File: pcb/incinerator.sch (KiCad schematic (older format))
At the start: 51 parts, among them J1 IGNITION_MAIN, J2 IGNITION_AFT, J3 VALVE_MAIN, J4 VALVE_AFT_HI, J5 Waveshare 4.2\" e-paper, J6 VALVE_AFT_LO, J7 AIRPMP, J8 Power Source 12V, Q1 IRLU120N, Q2 IRLU120N, Q3 IRLU120N, Q4 IRLU120N, Q5 IRLU120N, Q6 IRLU120N, SW1 Rotary_Encoder_Switch, U1 NodeMCU_ESP32, U2 Adafruit_MAX31855, U3 Adafruit_MAX31855, U4 R-7890-0.5

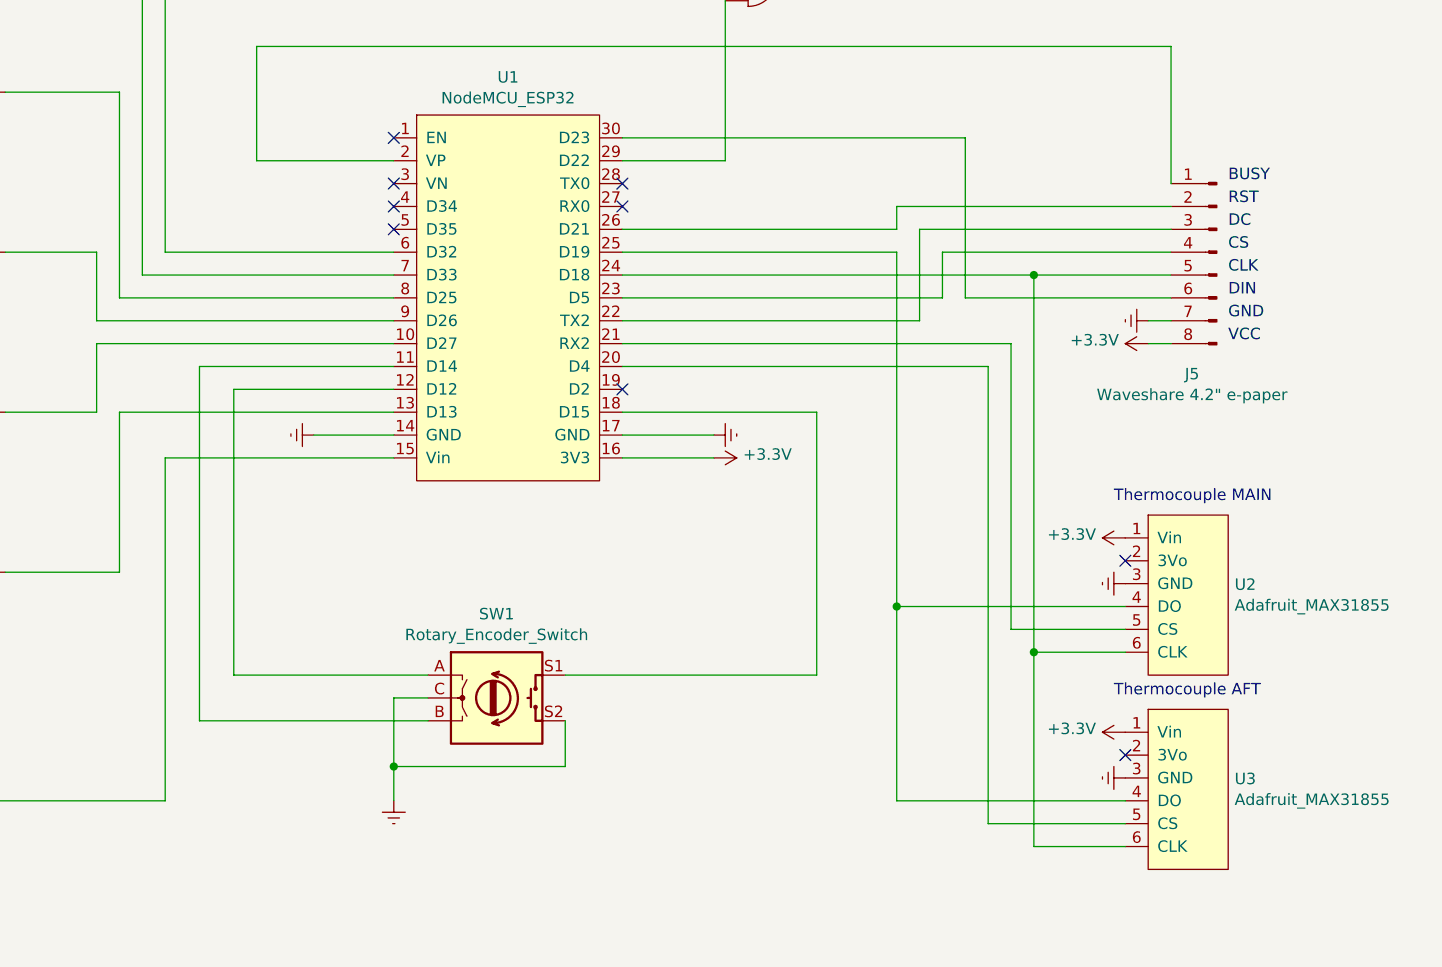
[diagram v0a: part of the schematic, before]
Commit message: Add connector to interface the encoder/switch
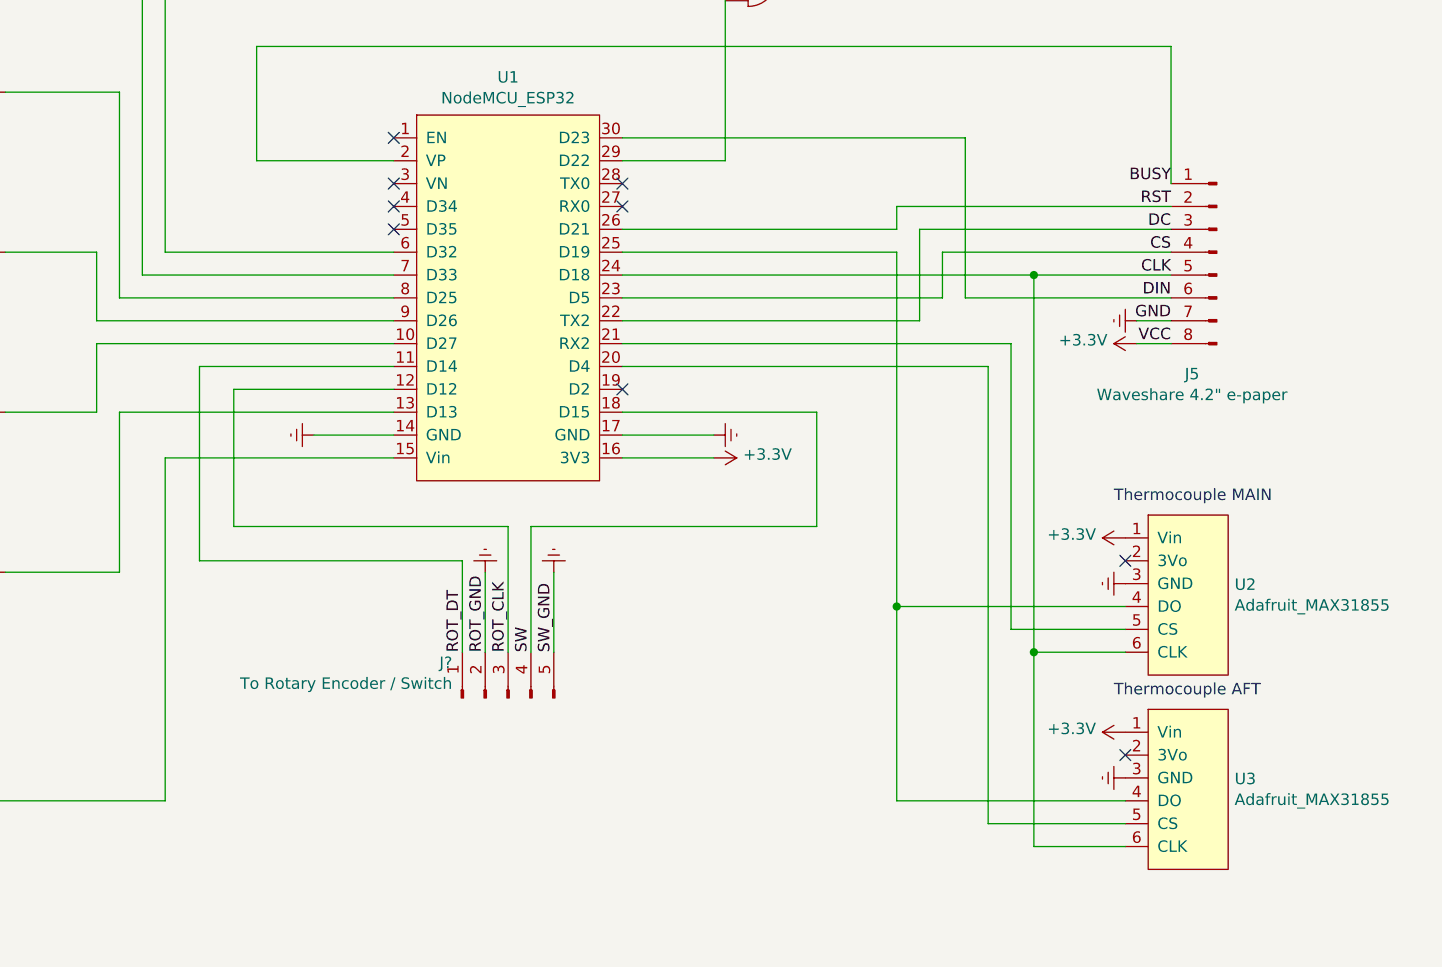
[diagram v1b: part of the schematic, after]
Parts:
- removed SW1: Rotary_Encoder_Switch, symbol Device:Rotary_Encoder_Switch
- added J?: To Rotary Encoder / Switch, symbol Connector:Conn_01x05_Male
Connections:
- net BUSY: now also J5.1 (Pin_1), U1.2 (VP)
- net CLK: now also J5.5 (Pin_5), U1.24 (D18), U2.6 (CLK), U3.6 (CLK)
- net CS: now also J5.4 (Pin_4), U1.23 (D5)
- net DC: now also J5.3 (Pin_3), U1.22 (TX2)
- net DIN: now also J5.6 (Pin_6), U1.30 (D23)
- net Earth: now also J?.2 (Pin_2), J?.5 (Pin_5)
- net RST: now also J5.2 (Pin_2), U1.26 (D21)
- net ROT_CLK: now reaches U1.12 (D12)
- net ROT_CLK: now also J?.3 (Pin_3)
- net ROT_DT: now reaches U1.11 (D14)
- net ROT_DT: now also J?.1 (Pin_1)
- net SW: now reaches U1.18 (D15)
- net SW: now also J?.4 (Pin_4)
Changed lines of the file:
@@
 Comment4 "Author: Patrick Huesmann"
 $EndDescr
-Text Label 10400 3350 0    50   ~ 0
+Text Label 10150 3350 2    50   ~ 0
 BUSY
-Text Label 10400 3450 0    50   ~ 0
+Text Label 10150 3450 2    50   ~ 0
 RST
-Text Label 10400 3550 0    50   ~ 0
+Text Label 10150 3550 2    50   ~ 0
 DC
-Text Label 10400 3650 0    50   ~ 0
+Text Label 10150 3650 2    50   ~ 0
 CS
-Text Label 10400 3750 0    50   ~ 0
+Text Label 10150 3750 2    50   ~ 0
 CLK
-Text Label 10400 3850 0    50   ~ 0
+Text Label 10150 3850 2    50   ~ 0
 DIN
-Text Label 10400 3950 0    50   ~ 0
+Text Label 10150 3950 2    50   ~ 0
 GND
-Text Label 10400 4050 0    50   ~ 0
+Text Label 10150 4050 2    50   ~ 0
 VCC
 Wire Wire Line
@@
 Wire Wire Line
 	9050 3550 9050 3950
-$Comp
-L Device:Rotary_Encoder_Switch SW1
-U 1 1 5DFF2455
-P 7200 5600
-F 0 "SW1" H 7200 5967 50  0000 C CNN
-F 1 "Rotary_Encoder_Switch" H 7200 5876 50  0000 C CNN
-F 2 "" H 7050 5760 50  0001 C CNN
-F 3 "~" H 7200 5860 50  0001 C CNN
-	1    7200 5600
-	1    0    0    -1
-$EndComp
-Wire Wire Line
-	6900 5600 6750 5600
-Wire Wire Line
-	6750 5600 6750 5900
-$Comp
-L power:Earth #PWR024
-U 1 1 5DFFCCE8
-P 6750 6050
-F 0 "#PWR024" H 6750 5800 50  0001 C CNN
-F 1 "Earth" H 6750 5900 50  0001 C CNN
-F 2 "" H 6750 6050 50  0001 C CNN
-F 3 "~" H 6750 6050 50  0001 C CNN
-	1    6750 6050
-	1    0    0    -1
-$EndComp
-Wire Wire Line
-	7500 5700 7500 5900
-Wire Wire Line
-	7500 5900 6750 5900
-Connection ~ 6750 5900
-Wire Wire Line
-	6750 5900 6750 6050
-Wire Wire Line
-	6900 5500 6050 5500
-Wire Wire Line
-	6900 5700 5900 5700
 Connection ~ 9550 3750
 Wire Wire Line
@@
 L power:Earth #PWR010
 U 1 1 5DEEEE26
-P 10050 3950
-F 0 "#PWR010" H 10050 3700 50  0001 C CNN
-F 1 "Earth" H 10050 3800 50  0001 C CNN
-F 2 "" H 10050 3950 50  0001 C CNN
-F 3 "~" H 10050 3950 50  0001 C CNN
-	1    10050 3950
-	0    1    1    0
-$EndComp
-Wire Wire Line
-	10050 3950 10150 3950
+P 10000 3950
+F 0 "#PWR010" H 10000 3700 50  0001 C CNN
+F 1 "Earth" H 10000 3800 50  0001 C CNN
+F 2 "" H 10000 3950 50  0001 C CNN
+F 3 "~" H 10000 3950 50  0001 C CNN
+	1    10000 3950
+	0    1    1    0
+$EndComp
+Wire Wire Line
+	10000 3950 10150 3950
 $Comp
 L Connector:Conn_01x08_Male J5
@@
 L power:+3.3V #PWR011
 U 1 1 5DEFD454
-P 10050 4050
-F 0 "#PWR011" H 10050 3900 50  0001 C CNN
-F 1 "+3.3V" V 10065 4178 50  0000 L CNN
-F 2 "" H 10050 4050 50  0001 C CNN
-F 3 "" H 10050 4050 50  0001 C CNN
-	1    10050 4050
-	0    -1   -1   0
-$EndComp
-Wire Wire Line
-	10050 4050 10150 4050
+P 10000 4050
+F 0 "#PWR011" H 10000 3900 50  0001 C CNN
+F 1 "+3.3V" V 10015 4178 50  0000 L CNN
+F 2 "" H 10000 4050 50  0001 C CNN
+F 3 "" H 10000 4050 50  0001 C CNN
+	1    10000 4050
+	0    -1   -1   0
+$EndComp
+Wire Wire Line
+	10000 4050 10150 4050
 $Comp
 L power:Earth #PWR019
@@
 $EndComp
 Wire Wire Line
-	8600 4350 8600 5500
-Wire Wire Line
-	7500 5500 8600 5500
+	8600 4350 8600 4850
 $Comp
 L power:+3.3V #PWR015
@@
 	6750 4250 6050 4250
 Wire Wire Line
-	6050 4250 6050 5500
+	6050 4250 6050 4850
 Wire Wire Line
 	6750 4150 5900 4150
-Wire Wire Line
-	5900 4150 5900 5700
 $Comp
 L Device:Q_NMOS_GDS Q1
@@
 NoConn ~ 7750 3450
 NoConn ~ 7750 3350
+$Comp
+L power:Earth #PWR?
+U 1 1 5E1FC7FA
+P 7150 5050
+F 0 "#PWR?" H 7150 4800 50  0001 C CNN
+F 1 "Earth" H 7150 4900 50  0001 C CNN
+F 2 "" H 7150 5050 50  0001 C CNN
+F 3 "~" H 7150 5050 50  0001 C CNN
+	1    7150 5050
+	-1   0    0    1
+$EndComp
+$Comp
+L power:Earth #PWR?
+U 1 1 5E1FD446
+P 7450 5050
+F 0 "#PWR?" H 7450 4800 50  0001 C CNN
+F 1 "Earth" H 7450 4900 50  0001 C CNN
+F 2 "" H 7450 5050 50  0001 C CNN
+F 3 "~" H 7450 5050 50  0001 C CNN
+	1    7450 5050
+	-1   0    0    1
+$EndComp
+Wire Wire Line
+	7450 5400 7450 5050
+Wire Wire Line
+	7150 5400 7150 5050
+Text Label 7050 5400 1    50   ~ 0
+ROT_DT
+Text Label 7250 5400 1    50   ~ 0
+ROT_CLK
+Text Label 7350 5400 1    50   ~ 0
+SW
+$Comp
+L Connector:Conn_01x05_Male J?
+U 1 1 5E1A7E2D
+P 7250 5600
+F 0 "J?" V 7404 5844 50  0000 L CNN
+F 1 "To Rotary Encoder / Switch" V 7313 5844 50  0000 L CNN
+F 2 "" H 7250 5600 50  0001 C CNN
+F 3 "~" H 7250 5600 50  0001 C CNN
+	1    7250 5600
+	0    -1   -1   0
+$EndComp
+Wire Wire Line
+	6050 4850 7250 4850
+Wire Wire Line
+	7250 4850 7250 5400
+Wire Wire Line
+	5900 5000 7050 5000
+Wire Wire Line
+	7050 5000 7050 5400
+Wire Wire Line
+	5900 4150 5900 5000
+Wire Wire Line
+	8600 4850 7350 4850
+Wire Wire Line
+	7350 4850 7350 5400
+Text Label 7150 5400 1    50   ~ 0
+ROT_GND
+Text Label 7450 5400 1    50   ~ 0
+SW_GND
 $EndSCHEMATC

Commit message: Re-annotated symbols
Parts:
- gave numbers to parts that had none: 1
- renumbered J8 to J9
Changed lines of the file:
@@
 	10000 4050 10150 4050
 $Comp
-L power:Earth #PWR019
+L power:Earth #PWR021
 U 1 1 5DF0E96B
 P 9950 5100
-F 0 "#PWR019" H 9950 4850 50  0001 C CNN
+F 0 "#PWR021" H 9950 4850 50  0001 C CNN
 F 1 "Earth" H 9950 4950 50  0001 C CNN
 F 2 "" H 9950 5100 50  0001 C CNN
@@
 $EndComp
 $Comp
-L power:Earth #PWR023
+L power:Earth #PWR025
 U 1 1 5DF11219
 P 9950 5950
-F 0 "#PWR023" H 9950 5700 50  0001 C CNN
+F 0 "#PWR025" H 9950 5700 50  0001 C CNN
 F 1 "Earth" H 9950 5800 50  0001 C CNN
 F 2 "" H 9950 5950 50  0001 C CNN
@@
 $EndComp
 $Comp
-L power:+3.3V #PWR021
+L power:+3.3V #PWR024
 U 1 1 5DF11220
 P 9950 5750
-F 0 "#PWR021" H 9950 5600 50  0001 C CNN
+F 0 "#PWR024" H 9950 5600 50  0001 C CNN
 F 1 "+3.3V" V 9965 5878 50  0000 L CNN
 F 2 "" H 9950 5750 50  0001 C CNN
@@
 Connection ~ 4100 1750
 $Comp
-L Connector:Screw_Terminal_01x02 J8
+L Connector:Screw_Terminal_01x02 J9
 U 1 1 5E156F2E
 P 1150 6050
-F 0 "J8" H 1068 6267 50  0000 C CNN
+F 0 "J9" H 1068 6267 50  0000 C CNN
 F 1 "Power Source 12V" H 1068 6176 50  0000 C CNN
 F 2 "" H 1150 6050 50  0001 C CNN
@@
 $EndComp
 $Comp
-L power:Earth #PWR025
+L power:Earth #PWR026
 U 1 1 5E159756
 P 1700 6600
-F 0 "#PWR025" H 1700 6350 50  0001 C CNN
+F 0 "#PWR026" H 1700 6350 50  0001 C CNN
 F 1 "Earth" H 1700 6450 50  0001 C CNN
 F 2 "" H 1700 6600 50  0001 C CNN
@@
 $EndComp
 $Comp
-L power:Earth #PWR020
+L power:Earth #PWR022
 U 1 1 5E319DD4
 P 4100 5350
-F 0 "#PWR020" H 4100 5100 50  0001 C CNN
+F 0 "#PWR022" H 4100 5100 50  0001 C CNN
 F 1 "Earth" H 4100 5200 50  0001 C CNN
 F 2 "" H 4100 5350 50  0001 C CNN
@@
 Connection ~ 1700 6350
 $Comp
-L power:PWR_FLAG #FLG0101
+L power:PWR_FLAG #FLG02
 U 1 1 5E1C89C2
 P 1700 6550
-F 0 "#FLG0101" H 1700 6625 50  0001 C CNN
+F 0 "#FLG02" H 1700 6625 50  0001 C CNN
 F 1 "PWR_FLAG" V 1700 6678 50  0000 L CNN
 F 2 "" H 1700 6550 50  0001 C CNN
@@
 	1700 6050 1700 5800
 $Comp
-L power:PWR_FLAG #FLG0102
+L power:PWR_FLAG #FLG01
 U 1 1 5E1C8CFC
 P 1700 5800
-F 0 "#FLG0102" H 1700 5875 50  0001 C CNN
+F 0 "#FLG01" H 1700 5875 50  0001 C CNN
 F 1 "PWR_FLAG" V 1700 5928 50  0000 L CNN
 F 2 "" H 1700 5800 50  0001 C CNN
@@
 $EndComp
 $Comp
-L power:+12V #PWR022
+L power:+12V #PWR023
 U 1 1 5E1590DD
 P 1700 5750
-F 0 "#PWR022" H 1700 5600 50  0001 C CNN
+F 0 "#PWR023" H 1700 5600 50  0001 C CNN
 F 1 "+12V" H 1715 5923 50  0000 C CNN
 F 2 "" H 1700 5750 50  0001 C CNN
@@
 NoConn ~ 7750 3350
 $Comp
-L power:Earth #PWR?
+L power:Earth #PWR019
 U 1 1 5E1FC7FA
 P 7150 5050
-F 0 "#PWR?" H 7150 4800 50  0001 C CNN
+F 0 "#PWR019" H 7150 4800 50  0001 C CNN
 F 1 "Earth" H 7150 4900 50  0001 C CNN
 F 2 "" H 7150 5050 50  0001 C CNN
@@
 $EndComp
 $Comp
-L power:Earth #PWR?
+L power:Earth #PWR020
 U 1 1 5E1FD446
 P 7450 5050
-F 0 "#PWR?" H 7450 4800 50  0001 C CNN
+F 0 "#PWR020" H 7450 4800 50  0001 C CNN
 F 1 "Earth" H 7450 4900 50  0001 C CNN
 F 2 "" H 7450 5050 50  0001 C CNN
@@
 SW
 $Comp
-L Connector:Conn_01x05_Male J?
+L Connector:Conn_01x05_Male J8
 U 1 1 5E1A7E2D
 P 7250 5600
-F 0 "J?" V 7404 5844 50  0000 L CNN
+F 0 "J8" V 7404 5844 50  0000 L CNN
 F 1 "To Rotary Encoder / Switch" V 7313 5844 50  0000 L CNN
 F 2 "" H 7250 5600 50  0001 C CNN

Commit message: Assigned footprints
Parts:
- BZ1: footprint (none) -> incinerator:Buzzer_BM_15B
- C1: footprint (none) -> Capacitor_THT:CP_Radial_D5.0mm_P2.50mm
- D1, D11, D3, D5, D7, D9: footprint (none) -> Diode_THT:D_DO-41_SOD81_P10.16mm_Horizontal
- D10, D12, D2, D4, D6, D8: footprint (none) -> LED_THT:LED_D3.0mm
- J1, J2, J3, J4, J6, J7, J9: footprint (none) -> TerminalBlock:TerminalBlock_bornier-2_P5.08mm
- J5: footprint (none) -> Connector_PinHeader_2.54mm:PinHeader_1x08_P2.54mm_Vertical
- J8: footprint (none) -> Connector_PinHeader_2.54mm:PinHeader_1x05_P2.54mm_Vertical
- Q1, Q2, Q3, Q4, Q5, Q6: footprint (none) -> Package_TO_SOT_THT:SIPAK_Vertical
- R1, R10, R11, R12, R13, R14, R15, R16, R17, R18, R2, R3, R4, R5, R6, R7, R8, R9: footprint (none) -> Resistor_THT:R_Axial_DIN0207_L6.3mm_D2.5mm_P10.16mm_Horizontal
- U1: footprint (none) -> incinerator:ESP32_NodeMCU
- U2, U3: footprint (none) -> incinerator:Adafruit_MAX31855

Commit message: started layout (WIP)
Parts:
- renumbered D8 to D10, D10 to D11, D3 to D2, D5 to D3, D7 to D4, D9 to D5, D11 to D6, D2 to D7, D4 to D8, D6 to D9, J9 to J1, J1 to J2, J2 to J3, J3 to J4, J4 to J5, J5 to J9, R12 to R10, R15 to R11, R18 to R12, R2 to R13, R5 to R14, R8 to R15, R11 to R16, R14 to R17, R17 to R18, R4 to R2, R7 to R3, R10 to R4, R13 to R5, R16 to R6, R3 to R7, R6 to R8, U4 to U1, U1 to U2, U2 to U3, U3 to U4

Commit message: First draft of PCB layout
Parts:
- removed D11, D9: GRN, LED_THT:LED_D3.0mm, symbol Device:LED
- removed D3, D5: D, Diode_THT:D_DO-41_SOD81_P10.16mm_Horizontal, symbol Device:D
- added D11, D9: D, Diode_THT:D_DO-41_SOD81_P10.16mm_Horizontal, symbol Device:D
- added D3, D5: RED, LED_THT:LED_D3.0mm, symbol Device:LED
- D10: value GRN -> RED
- D12: value YLW -> RED
- R11, R8: value 15k -> 100
- R12, R9: value 15k -> 1k
- R14, R17: value 100 -> 15k
- R16: value 100 -> 1k
- R3, R6: value 1k -> 15k
- R4: value 1k -> 100
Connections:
- net +12V: now also R12.2, R16.2, R9.2, D11.1 (K), D9.1 (K); no longer R3.2, R4.2, R6.2
- net Earth: now also R14.1, R17.1, R3.1, R6.1; no longer R11.1, R12.1, R8.1, R9.1
- net at U2.10 (D27): now also R15.2; no longer R17.2
- net at U2.7 (D33): now also R4.2; no longer R14.2
- net at U2.8 (D25): now also R8.2; no longer R15.2
- net at U2.9 (D26): now also R11.2; no longer R16.2
- net at D2.2 (A), J3.2 (Pin_2), Q2.2 (D): now also D3.1 (K); no longer D8.1 (K)
- net at R2.1: now also D3.2 (A); no longer D8.2 (A)
- net at J4.2 (Pin_2), Q3.2 (D): now also D4.2 (A), D5.1 (K)
- net at Q4.1 (G), R10.2: now also R11.1; no longer R16.1
- net at J5.2 (Pin_2), Q4.2 (D): now also D6.2 (A), D8.1 (K); no longer D10.1 (K), D4.2 (A)
- net at R4.1: now also Q2.1 (G), R3.2; no longer D10.2 (A)
- net at J6.2 (Pin_2), Q5.2 (D): now also D10.1 (K), D9.2 (A)
- net at R5.1: now also D5.2 (A)
- net at Q6.1 (G), R18.1: now also R17.2; no longer R12.2
- net at D12.1 (K), J7.2 (Pin_2), Q6.2 (D): now also D11.2 (A); no longer D6.2 (A)
- net at D12.2 (A): now also R16.1; no longer R6.1
- new net: Q3.1 (G), R6.2, R8.1
- new net: D8.2 (A), R9.1
- new net: Q5.1 (G), R14.2, R15.1
- new net: D10.2 (A), R12.1
